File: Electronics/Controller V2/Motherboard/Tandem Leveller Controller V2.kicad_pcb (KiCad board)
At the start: 6 copper layers, 230.5 x 129 mm, 84 parts, among them J1 Conn_01x08, J10 ORIENT, J11 OPT, J12 IMU, J14 TABLET 1 PWR, J15 TABLET 2 PWR, J2 Conn_01x10, J3 GNSS, J4 TERM, J5 Pulse_J0011D01BNL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

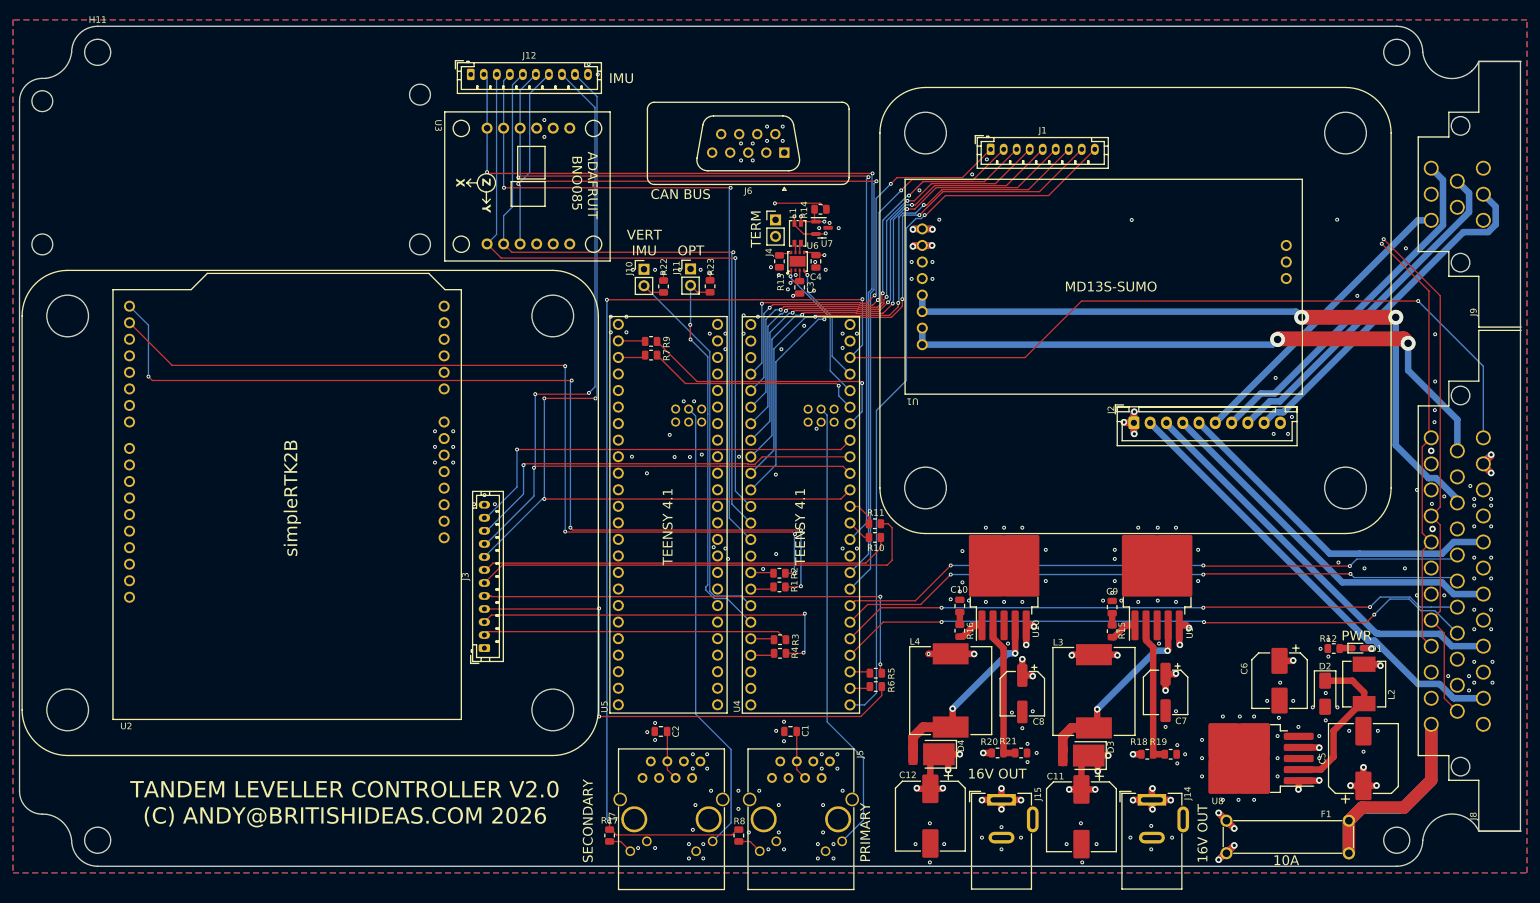
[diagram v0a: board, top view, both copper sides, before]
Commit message: Added WAS circuit.
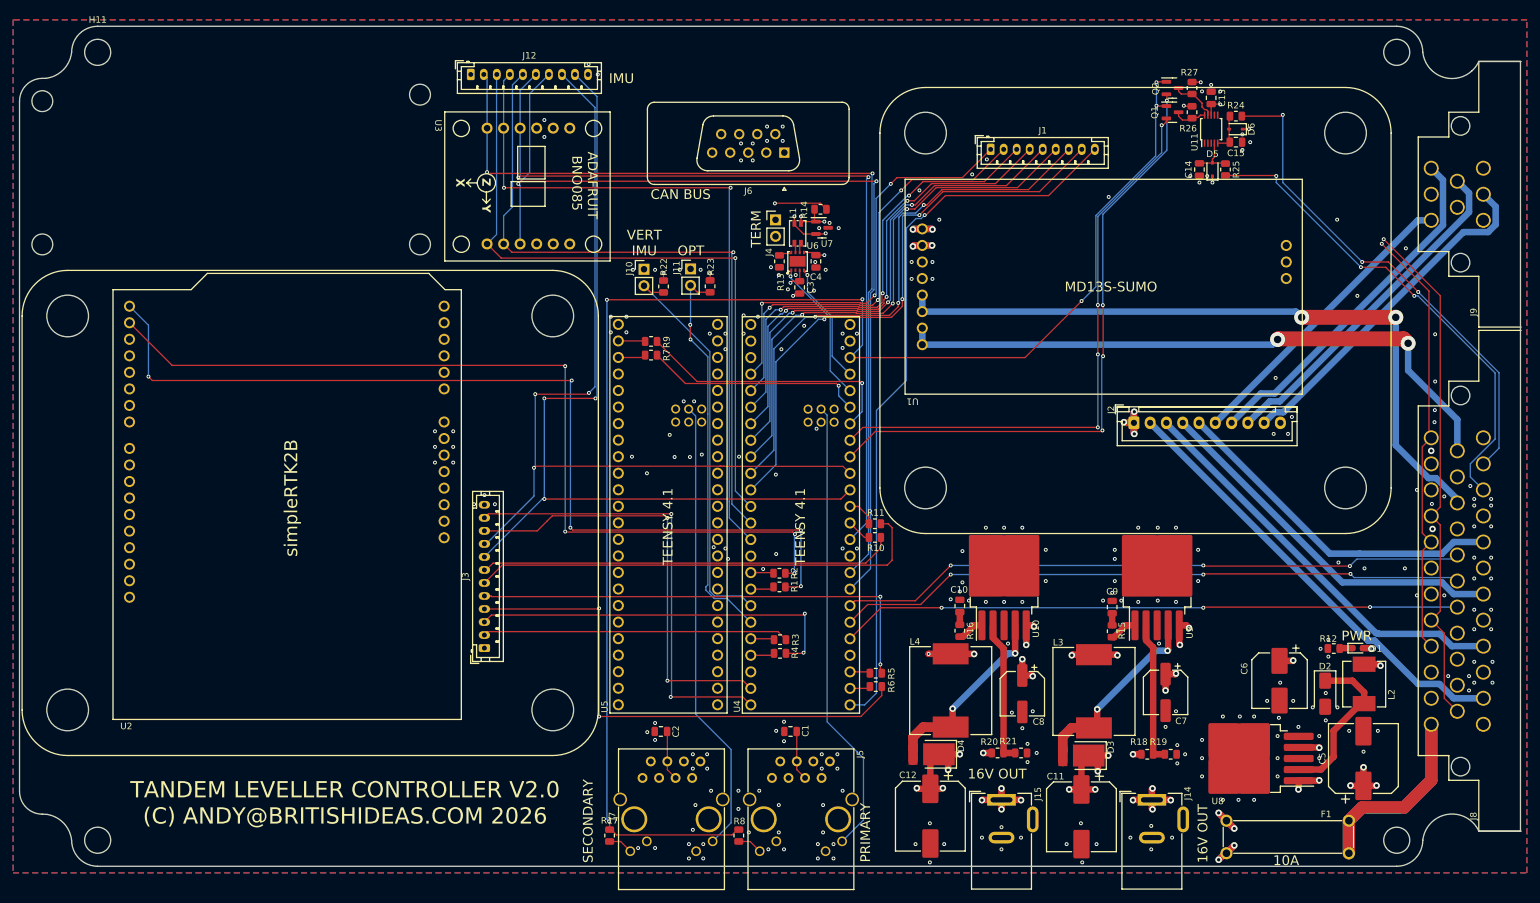
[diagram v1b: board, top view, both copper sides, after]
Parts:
- added C13: 100n, Capacitor_SMD:C_0805_2012Metric, F.Cu at (210.0, 35.0)
- added C14: 10n, Capacitor_SMD:C_0805_2012Metric, F.Cu at (208.2, 46.0)
- added C15: 10n, Capacitor_SMD:C_0805_2012Metric, F.Cu at (213.8, 41.8)
- added D5: 1N5819WS, Diode_SMD:D_SOD-323, F.Cu at (210.2, 46.0)
- added D6: 1N5819WS, Diode_SMD:D_SOD-323, F.Cu at (213.8, 39.8)
- added Q1: 2N7002, Package_TO_SOT_SMD:SOT-23, F.Cu at (204.1, 37.2)
- added Q2: 2N7002, Package_TO_SOT_SMD:SOT-23, F.Cu at (204.1, 33.5)
- added R24: 1k5, Resistor_SMD:R_0805_2012Metric, F.Cu at (213.8, 37.8)
- added R25: 1k5, Resistor_SMD:R_0805_2012Metric, F.Cu at (212.2, 46.0)
- added R26: 5k1, Resistor_SMD:R_0805_2012Metric, F.Cu at (207.1, 37.2)
- added R27: 5k1, Resistor_SMD:R_0805_2012Metric, F.Cu at (207.1, 33.5)
- added U11: ADS1115IDGS, Package_SO:TSSOP-10_3x3mm_P0.5mm, F.Cu at (210.0, 39.8)
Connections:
- J8 pad 16: /GPIO_C4 -> +5V
- J8 pad 33: GND -> /Autosteer/WAS_H
- J8 pad 34: +12V -> /Autosteer/WAS_L
- J8 pad 35: +3V3 -> GND
- U4 pad 23: unconnected-(U4-GPIO31_CTX3-Pad23) -> /GNSS/GPIO_G3
- U4 pad 24: unconnected-(U4-GPIO32-Pad24) -> /GNSS/GPIO_G4
- U4 pad 28: /GPIO_C4 -> unconnected-(U4-GPIO36_CS-Pad28)
- U4 pad 40: /GNSS/GPIO_G3 -> /Autosteer/WAS_SDA
- U4 pad 41: /GNSS/GPIO_G4 -> /Autosteer/WAS_SCL
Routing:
- net /GPIO_C4: track 99.2 -> 0.00 mm, vias 3 -> 0
- net /Autosteer/WAS_SDA: track 0.00 -> 96.3 mm, vias 0 -> 4
- net /Autosteer/WAS_SCL: track 0.00 -> 90.8 mm, vias 0 -> 4
- net /Autosteer/WAS_L: track 0.00 -> 77.7 mm, vias 0 -> 3
- net /Autosteer/WAS_H: track 0.00 -> 74.9 mm, vias 0 -> 3
- net +3V3: track 267.1 -> 231.7 mm, vias 4 -> 6
- net +5V: track 18.0 -> 25.6 mm, vias 8 -> 13
- net +12V: track 86.0 -> 78.4 mm, vias 30 -> 28
- net Net-(Q2-D): track 0.00 -> 7.25 mm
- net Net-(D5-A): track 0.00 -> 7.22 mm
- net Net-(D6-A): track 0.00 -> 6.01 mm
- net /GNSS/GPIO_G4: track 64.5 -> 70.3 mm, vias 1 -> 2
- net Net-(Q1-D): track 0.00 -> 5.16 mm
- net /GNSS/GPIO_G3: track 63.5 -> 67.8 mm, vias 1 -> 2
- net /CAN_L: track 186.1 -> 188.9 mm
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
